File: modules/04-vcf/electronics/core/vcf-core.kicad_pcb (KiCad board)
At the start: 2 copper layers, 58 x 65 mm, 88 parts, among them J1 Conn_01x06, J2 Conn_02x04_Counter_Clockwise, J3 Conn_02x02_Counter_Clockwise, J4 S1711-46R, J5 S1711-46R, J6 Conn_02x03_Odd_Even, J7 Conn_01x02, J8 Conn_02x05_Odd_Even, Q1 BC847BS, U1 TL072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

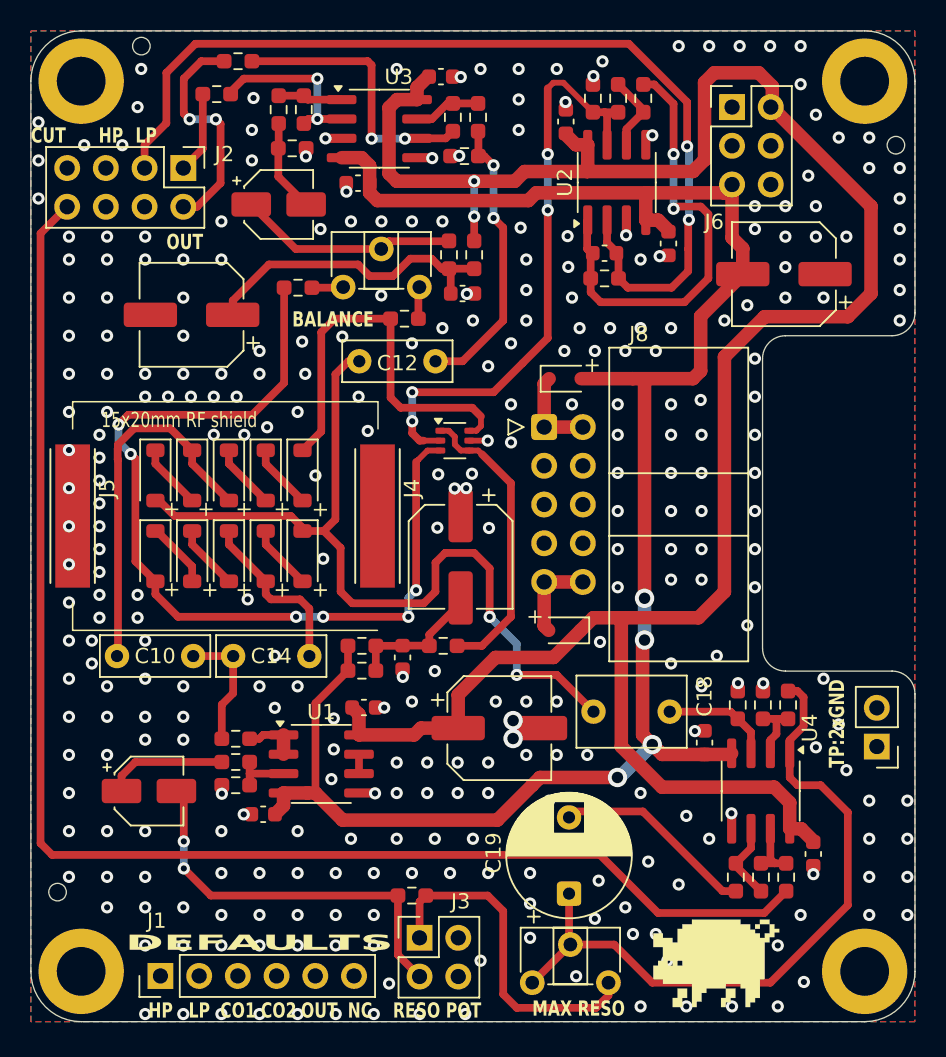
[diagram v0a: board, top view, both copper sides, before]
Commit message: VCF JLCPCB verified for v1.0
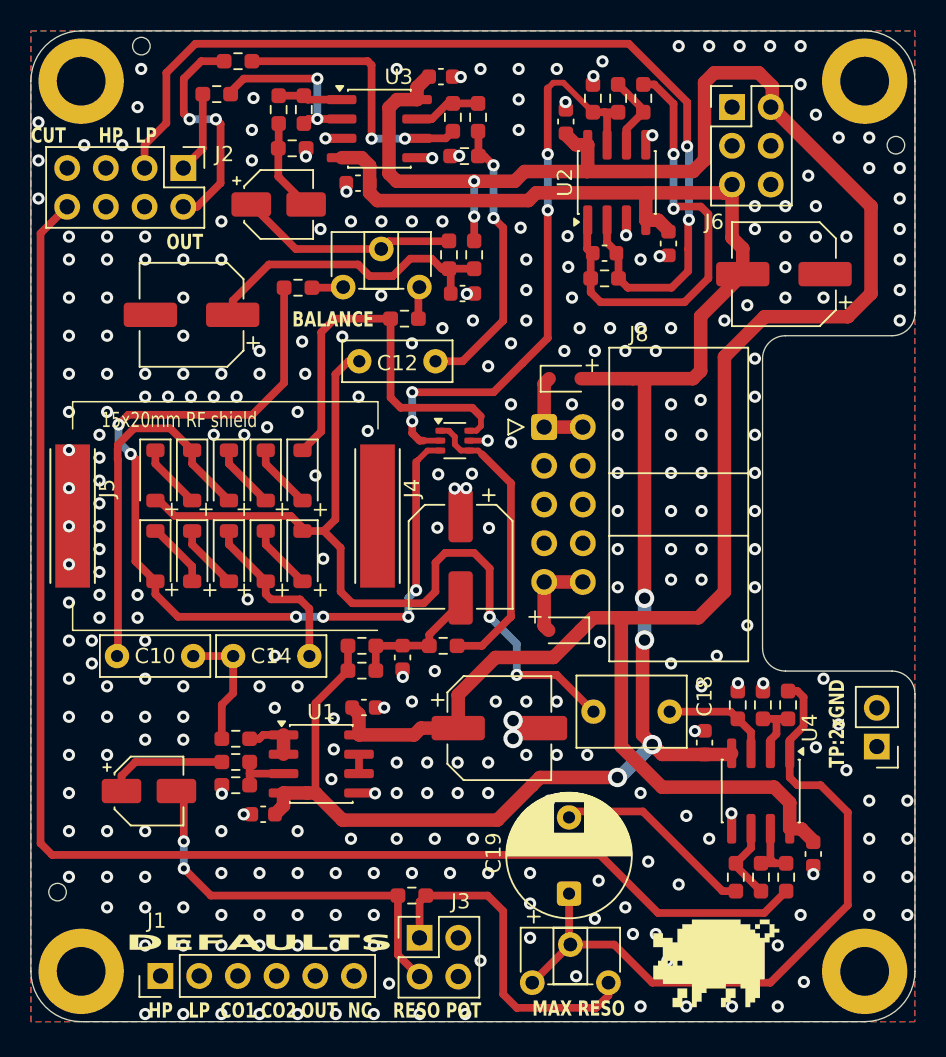
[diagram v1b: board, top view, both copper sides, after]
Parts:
- added G***: LOGO, Shmoergh_Custom_Footprints:Gyeszno, B.Cu at (136.2, 108.1)
- C19: value 10u -> 4.7u
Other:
- board text added: "SHMØERGH MODULEUR"
- board text added: "SM-04 Diode Filter V1.0 2025 Dec"
- board text removed: "HM-04 Diode Filter V0.2 2025 July"
- board text removed: "SHMØERGH HOG MODULEUR"

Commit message: KiCAD version update - VCF
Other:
- board text added: "SM-04 Diode Filter V1.0"
- board text removed: "SM-04 Diode Filter V1.0 2025 Dec"

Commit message: Cleanup
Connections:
- net Net-(C10-Pad2) renamed /VCF/FEEDBACK
- net Net-(C11-Pad1) renamed /VCF/LP_I
- net Net-(C12-Pad2) renamed /VCF/HP_I
- net Net-(D5-A) renamed /VCF/D_OUT
- net Net-(Q1A-B1) renamed /VCF/CV_I

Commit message: Changed board versioning to 'rev' on VCF
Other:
- board text added: "Diode Filter REV 1"
- board text removed: "SM-04 Diode Filter V1.0"
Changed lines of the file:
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@@
 		)
 	)
-	(gr_text "SM-04 \nDiode Filter\nV1.0"
+	(gr_text "Diode Filter\nREV 1"
 		(at 140.383 124.899 0)
 		(layer "B.SilkS")
@@
 			(justify left bottom mirror)
 		)
-		(render_cache "SM-04 \nDiode Filter\nV1.0" 0
-			(polygon
-				(pts
-					(xy 140.236661 119.810498) (xy 140.236661 120.107739) (xy 140.085829 120.107739) (xy 140.085829 119.810498)
-				)
-			)
-			(polygon
-				(pts
-					(xy 140.090323 120.103245) (xy 140.090323 120.254077) (xy 139.646745 120.254077) (xy 139.646745 120.103245)
-				)
-			)
-			(polygon
-				(pts
-					(xy 139.646745 120.688667) (xy 140.090323 120.688667) (xy 140.090323 120.8395) (xy 139.646745 120.8395)
-				)
-			)
-			(polygon
-				(pts
-					(xy 140.085829 120.693161) (xy 140.085829 120.542329) (xy 140.236661 120.542329) (xy 140.236661 120.693161)
-				)
-			)
-			(polygon
-				(pts
-					(xy 139.651239 120.249583) (xy 139.651239 120.693161) (xy 139.500336 120.693161) (xy 139.500336 120.249583)
-				)
-			)
-			(polygon
-				(pts
-					(xy 140.090323 119.66409) (xy 140.090323 119.814992) (xy 139.646745 119.814992) (xy 139.646745 119.66409)
-				)
-			)
-			(polygon
-				(pts
-					(xy 139.651239 119.810498) (xy 139.651239 119.96133) (xy 139.500336 119.96133) (xy 139.500336 119.810498)
-				)
-			)
-			(polygon
-				(pts
-					(xy 139.213137 119.66409) (xy 139.213137 120.8395) (xy 139.062305 120.8395) (xy 139.062305 120.107739)
-					(xy 138.915897 120.107739) (xy 138.915897 119.956836) (xy 139.062305 119.956836) (xy 139.062305 119.66409)
-				)
-			)
-			(polygon
-				(pts
-					(xy 138.627715 120.107739) (xy 138.627715 120.8395) (xy 138.476812 120.8395) (xy 138.476812 119.66409)
-					(xy 138.627715 119.66409) (xy 138.627715 119.956836) (xy 138.774053 119.956836) (xy 138.774053 120.107739)
-				)
-			)
-			(polygon
-				(pts
-					(xy 138.920391 120.103245) (xy 138.920391 120.400415) (xy 138.769559 120.400415) (xy 138.769559 120.103245)
-				)
-			)
-			(polygon
-				(pts
-					(xy 137.599697 120.249583) (xy 138.043275 120.249583) (xy 138.043275 120.400415) (xy 137.599697 120.400415)
-				)
-			)
-			(polygon
-				(pts
-					(xy 137.166089 119.810498) (xy 137.166089 120.693161) (xy 137.015257 120.693161) (xy 137.015257 120.400415)
-					(xy 136.868849 120.400415) (xy 136.868849 120.249583) (xy 137.015257 120.249583) (xy 137.015257 119.810498)
-				)
-			)
-			(polygon
-				(pts
-					(xy 137.019751 120.688667) (xy 137.019751 120.8395) (xy 136.576172 120.8395) (xy 136.576172 120.688667)
-				)
-			)
-			(polygon
-				(pts
-					(xy 137.019751 119.66409) (xy 137.019751 119.814992) (xy 136.576172 119.814992) (xy 136.576172 119.66409)
-				)
-			)
-			(polygon
-				(pts
-					(xy 136.580667 119.810498) (xy 136.580667 119.956836) (xy 136.727005 119.956836) (xy 136.727005 120.107739)
-					(xy 136.580667 120.107739) (xy 136.580667 120.693161) (xy 136.429764 120.693161) (xy 136.429764 119.810498)
-				)
-			)
-			(polygon
-				(pts
-					(xy 136.873343 120.103245) (xy 136.873343 120.254077) (xy 136.722511 120.254077) (xy 136.722511 120.103245)
-				)
-			)
-			(polygon
-				(pts
-					(xy 135.703481 119.66409) (xy 135.703481 119.814992) (xy 135.557142 119.814992) (xy 135.557142 120.395921)
-					(xy 135.991733 120.395921) (xy 135.991733 120.103245) (xy 136.142565 120.103245) (xy 136.142565 120.546823)
-					(xy 135.557142 120.546823) (xy 135.557142 120.8395) (xy 135.40624 120.8395) (xy 135.40624 119.66409)
-				)
-			)
-			(polygon
-				(pts
-					(xy 135.849819 119.810498) (xy 135.849819 119.96133) (xy 135.698987 119.96133) (xy 135.698987 119.810498)
-				)
-			)
-			(polygon
-				(pts
-					(xy 135.996227 119.956836) (xy 135.996227 120.107739) (xy 135.845325 120.107739) (xy 135.845325 119.956836)
-				)
-			)
+		(render_cache "Diode Filter\nREV 1" 0
 			(polygon
 				(pts
@@
 			(polygon
 				(pts
-					(xy 139.939421 124.557161) (xy 139.939421 124.259921) (xy 140.090323 124.259921) (xy 140.090323 124.557161)
-				)
-			)
-			(polygon
-				(pts
-					(xy 139.943915 124.552667) (xy 139.943915 124.7035) (xy 139.793083 124.7035) (xy 139.793083 124.552667)
-				)
-			)
-			(polygon
-				(pts
-					(xy 140.236661 123.52809) (xy 140.236661 124.264415) (xy 140.085829 124.264415) (xy 140.085829 123.52809)
-				)
-			)
-			(polygon
-				(pts
-					(xy 139.651239 123.52809) (xy 139.651239 124.264415) (xy 139.500336 124.264415) (xy 139.500336 123.52809)
-				)
-			)
-			(polygon
-				(pts
-					(xy 139.797577 124.259921) (xy 139.797577 124.557161) (xy 139.646745 124.557161) (xy 139.646745 124.259921)
-				)
-			)
-			(polygon
-				(pts
-					(xy 138.920391 123.82533) (xy 138.920391 124.552667) (xy 139.213137 124.552667) (xy 139.213137 124.7035)
-					(xy 138.476812 124.7035) (xy 138.476812 124.552667) (xy 138.769559 124.552667) (xy 138.769559 123.52809)
-					(xy 138.920391 123.52809) (xy 138.920391 123.674498) (xy 139.213137 123.674498) (xy 139.213137 123.82533)
-				)
-			)
-			(polygon
-				(pts
-					(xy 137.896867 124.406329) (xy 137.896867 124.7035) (xy 137.746035 124.7035) (xy 137.746035 124.406329)
-				)
-			)
-			(polygon
-				(pts
-					(xy 137.166089 123.674498) (xy 137.166089 124.557161) (xy 137.015257 124.557161) (xy 137.015257 124.264415)
-					(xy 136.868849 124.264415) (xy 136.868849 124.113583) (xy 137.015257 124.113583) (xy 137.015257 123.674498)
-				)
-			)
-			(polygon
-				(pts
-					(xy 137.019751 124.552667) (xy 137.019751 124.7035) (xy 136.576172 124.7035) (xy 136.576172 124.552667)
-				)
-			)
-			(polygon
-				(pts
-					(xy 137.019751 123.52809) (xy 137.019751 123.678992) (xy 136.576172 123.678992) (xy 136.576172 123.52809)
-				)
-			)
-			(polygon
-				(pts
-					(xy 136.580667 123.674498) (xy 136.580667 123.820836) (xy 136.727005 123.820836) (xy 136.727005 123.971739)
-					(xy 136.580667 123.971739) (xy 136.580667 124.557161) (xy 136.429764 124.557161) (xy 136.429764 123.674498)
-				)
-			)
-			(polygon
-				(pts
-					(xy 136.873343 123.967245) (xy 136.873343 124.118077) (xy 136.722511 124.118077) (xy 136.722511 123.967245)
-				)
-			)
+					(xy 140.236661 123.52809) (xy 140.236661 124.7035) (xy 140.085829 124.7035) (xy 140.085829 124.264415)
+					(xy 139.797577 124.264415) (xy 139.797577 124.410823) (xy 139.646745 124.410823) (xy 139.646745 124.113583)
+					(xy 140.085829 124.113583) (xy 140.085829 123.678992) (xy 139.646745 123.678992) (xy 139.646745 123.52809)
+				)
+			)
+			(polygon
+				(pts
+					(xy 139.651239 123.674498) (xy 139.651239 124.118077) (xy 139.500336 124.118077) (xy 139.500336 123.674498)
+				)
+			)
+			(polygon
+				(pts
+					(xy 139.651239 124.406329) (xy 139.651239 124.7035) (xy 139.500336 124.7035) (xy 139.500336 124.406329)
+				)
+			)
+			(polygon
+				(pts
+					(xy 139.213137 123.52809) (xy 139.213137 124.7035) (xy 138.476812 124.7035) (xy 138.476812 124.552667)
+					(xy 139.062305 124.552667) (xy 139.062305 124.118077) (xy 138.623221 124.118077) (xy 138.623221 123.967245)
+					(xy 139.062305 123.967245) (xy 139.062305 123.678992) (xy 138.476812 123.678992) (xy 138.476812 123.52809)
+				)
+			)
+			(polygon
+				(pts
+					(xy 137.892373 124.557161) (xy 137.892373 124.259921) (xy 138.043275 124.259921) (xy 138.043275 124.557161)
+				)
+			)
+			(polygon
+				(pts
+					(xy 137.896867 124.552667) (xy 137.896867 124.7035) (xy 137.746035 124.7035) (xy 137.746035 124.552667)
+				)
+			)
+			(polygon
+				(pts
+					(xy 138.189613 123.52809) (xy 138.189613 124.264415) (xy 138.038781 124.264415) (xy 138.038781 123.52809)
+				)
+			)
+			(polygon
+				(pts
+					(xy 137.604191 123.52809) (xy 137.604191 124.264415) (xy 137.453288 124.264415) (xy 137.453288 123.52809)
+				)
+			)
+			(polygon
+				(pts
+					(xy 137.750529 124.259921) (xy 137.750529 124.557161) (xy 137.599697 124.557161) (xy 137.599697 124.259921)
+				)
+			)
+			(polygon
+				(pts
+					(xy 135.849819 123.82533) (xy 135.849819 124.552667) (xy 136.142565 124.552667) (xy 136.142565 124.7035)
+					(xy 135.40624 124.7035) (xy 135.40624 124.552667) (xy 135.698987 124.552667) (xy 135.698987 123.52809)
+					(xy 135.849819 123.52809) (xy 135.849819 123.674498) (xy 136.142565 123.674498) (xy 136.142565 123.82533)
+				)
+			)

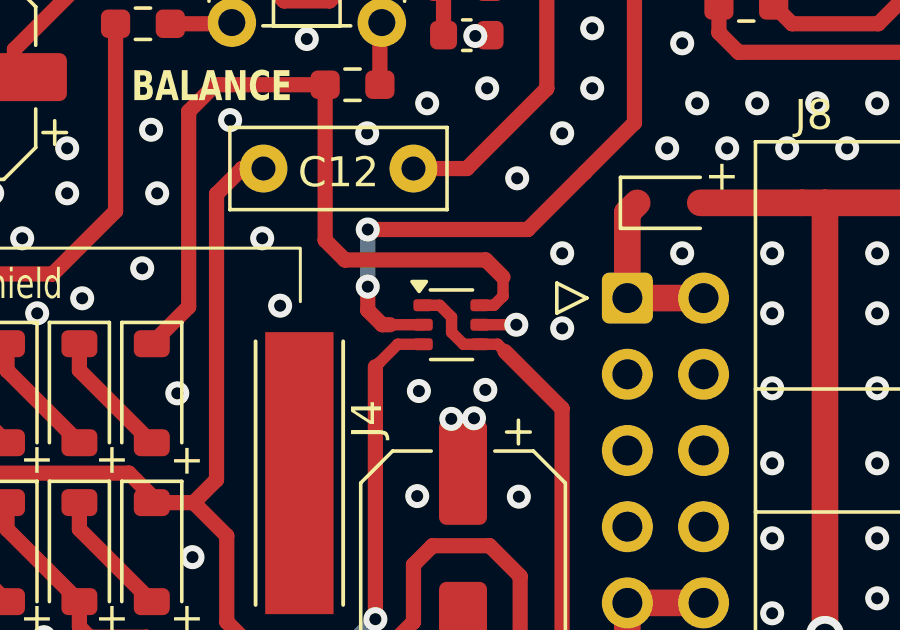
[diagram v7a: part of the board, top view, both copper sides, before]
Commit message: Fixed VCF Core schemo and PCB after fckckin KiCAD update
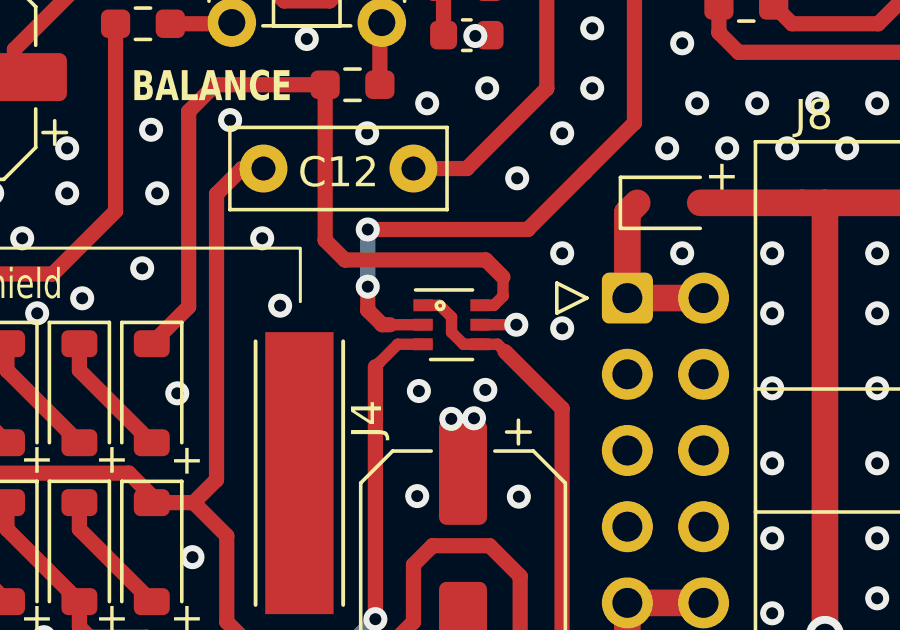
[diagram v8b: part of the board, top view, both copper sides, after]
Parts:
- Q1: footprint Package_TO_SOT_SMD:SOT-363_SC-70-6 -> Shmoergh_Custom_Footprints:SOT-363_SC-70-6
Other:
- board text added: "Diode Filter REV 2"
- board text removed: "Diode Filter REV 1"
